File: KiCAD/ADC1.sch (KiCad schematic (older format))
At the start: 26 parts, among them J1 Conn_02x08_Odd_Even, J2 Conn_02x08_Odd_Even, J3 Conn_02x08_Odd_Even, J4 Conn_02x08_Odd_Even, U1 AD7779

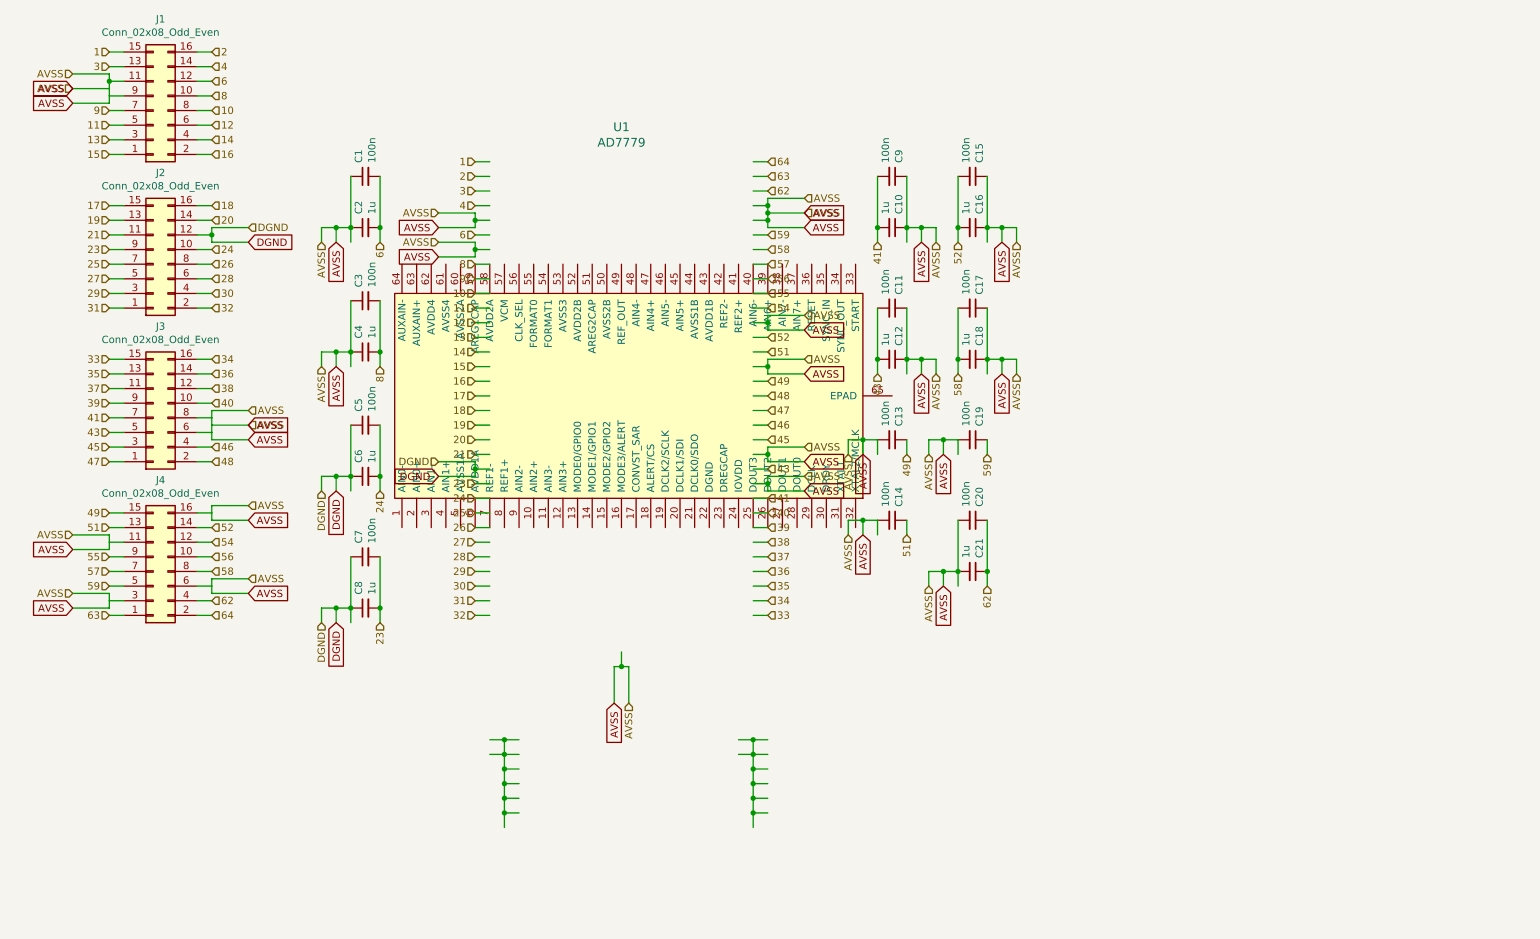
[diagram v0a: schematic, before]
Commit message: added usb, crystals
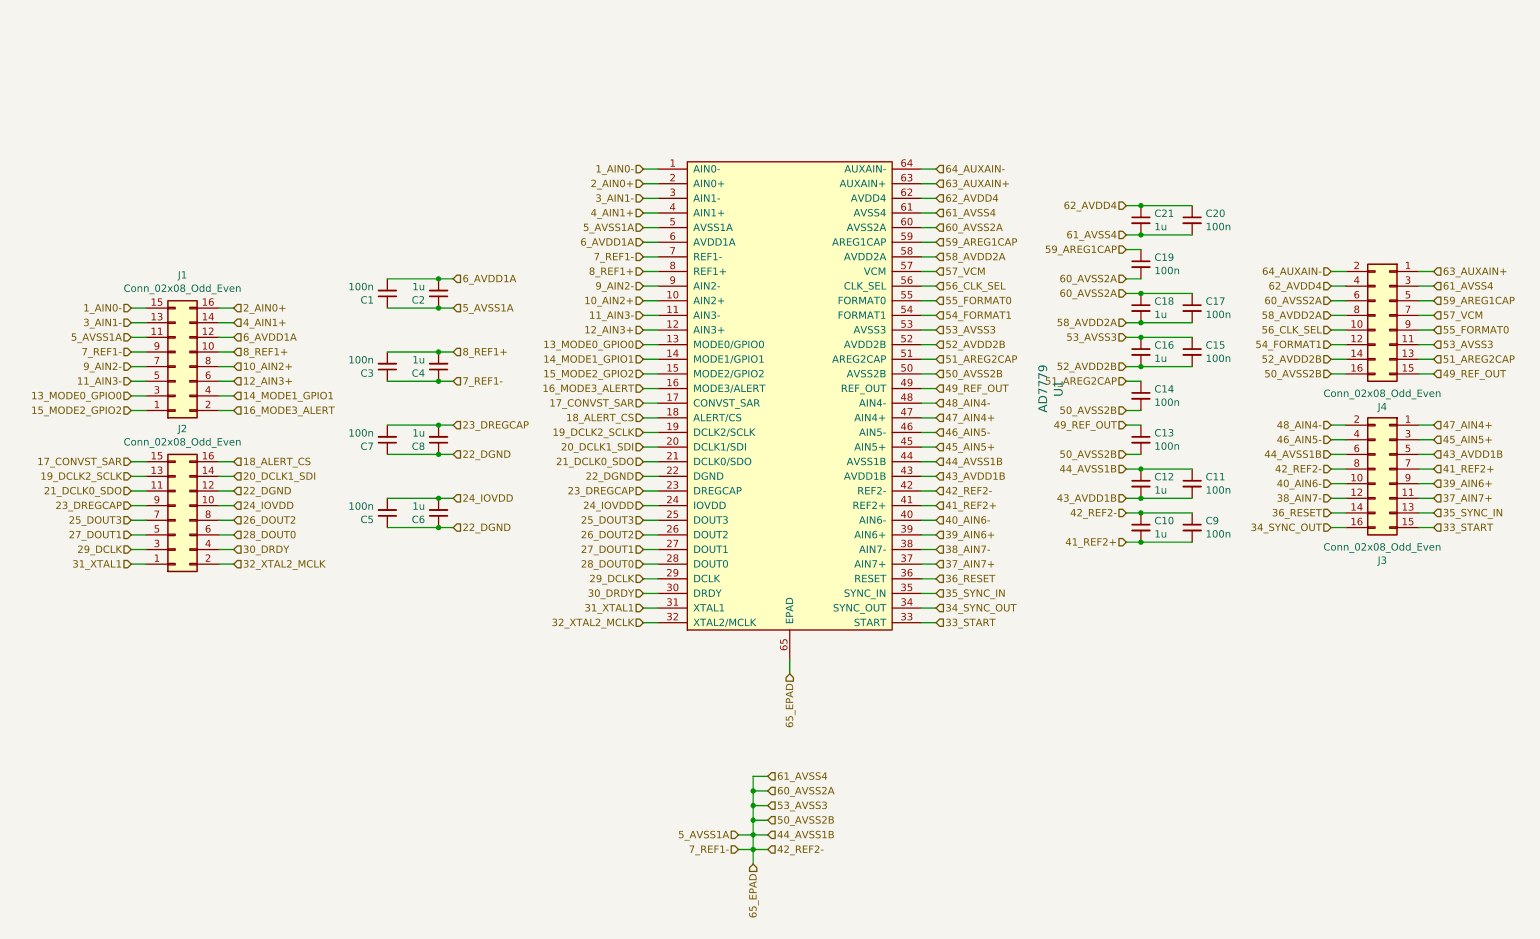
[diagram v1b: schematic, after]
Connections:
- net labels added: 10_AIN2+, 11_AIN3-, 12_AIN3+, 13_MODE0_GPIO0, 14_MODE1_GPIO1, 15_MODE2_GPIO2, 16_MODE3_ALERT, 17_CONVST_SAR, 18_ALERT_CS, 19_DCLK2_SCLK, 1_AIN0-, 20_DCLK1_SDI, 21_DCLK0_SDO, 22_DGND, 23_DREGCAP, 24_IOVDD, 25_DOUT3, 26_DOUT2, 27_DOUT1, 28_DOUT0, 29_DCLK, 2_AIN0+, 30_DRDY, 31_XTAL1, 32_XTAL2_MCLK, 33_START, 34_SYNC_OUT, 35_SYNC_IN, 36_RESET, 37_AIN7+, 38_AIN7-, 39_AIN6+, 3_AIN1-, 40_AIN6-, 41_REF2+, 42_REF2-, 43_AVDD1B, 44_AVSS1B, 45_AIN5+, 46_AIN5-, 47_AIN4+, 48_AIN4-, 49_REF_OUT, 4_AIN1+, 50_AVSS2B, 51_AREG2CAP, 52_AVDD2B, 53_AVSS3, 54_FORMAT1, 55_FORMAT0, 56_CLK_SEL, 57_VCM, 58_AVDD2A, 59_AREG1CAP, 5_AVSS1A, 60_AVSS2A, 61_AVSS4, 62_AVDD4, 63_AUXAIN+, 64_AUXAIN-, 65_EPAD, 6_AVDD1A, 7_REF1-, 8_REF1+, 9_AIN2-
- net labels removed: 1, 10, 11, 12, 13, 14, 15, 16, 17, 18, 19, 2, 20, 21, 23, 24, 25, 26, 27, 28, 29, 3, 30, 31, 32, 33, 34, 35, 36, 37, 38, 39, 4, 40, 41, 43, 45, 46, 47, 48, 49, 51, 52, 54, 55, 56, 57, 58, 59, 6, 62, 63, 64, 8, 9, AVSS, DGND
- wire segments 320 -> 185
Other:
- moved on the sheet: C1, C10, C11, C12, C13, C14, C15, C16, C17, C18, C19, C2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
